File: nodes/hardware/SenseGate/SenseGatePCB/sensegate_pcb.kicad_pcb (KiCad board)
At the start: 2 copper layers, 110.1 x 110.1 mm, 24 parts, among them J3 Conn_01x02_Socket, J4 Conn_01x24_Pin, J5 Conn_01x04_Socket, J6 Conn_01x04_Socket, J7 Conn_01x04_Socket, J8 Conn_01x04_Socket, J9 Conn_01x04_Socket, Q4 SS8050, U1 DD05CVSA, U2 mt3608_dcdc_converter

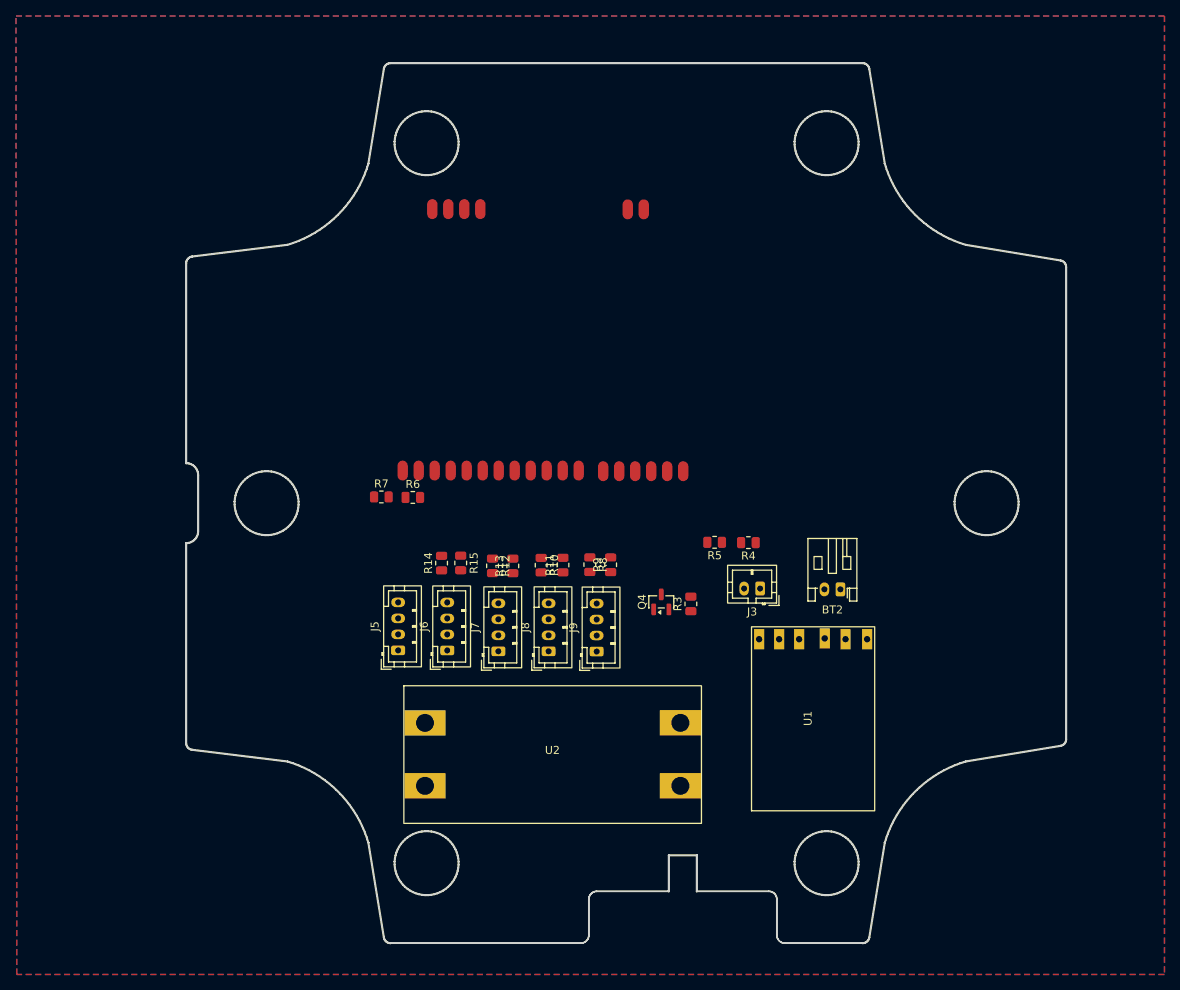
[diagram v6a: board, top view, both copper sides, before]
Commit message: pcb needs only wiring now
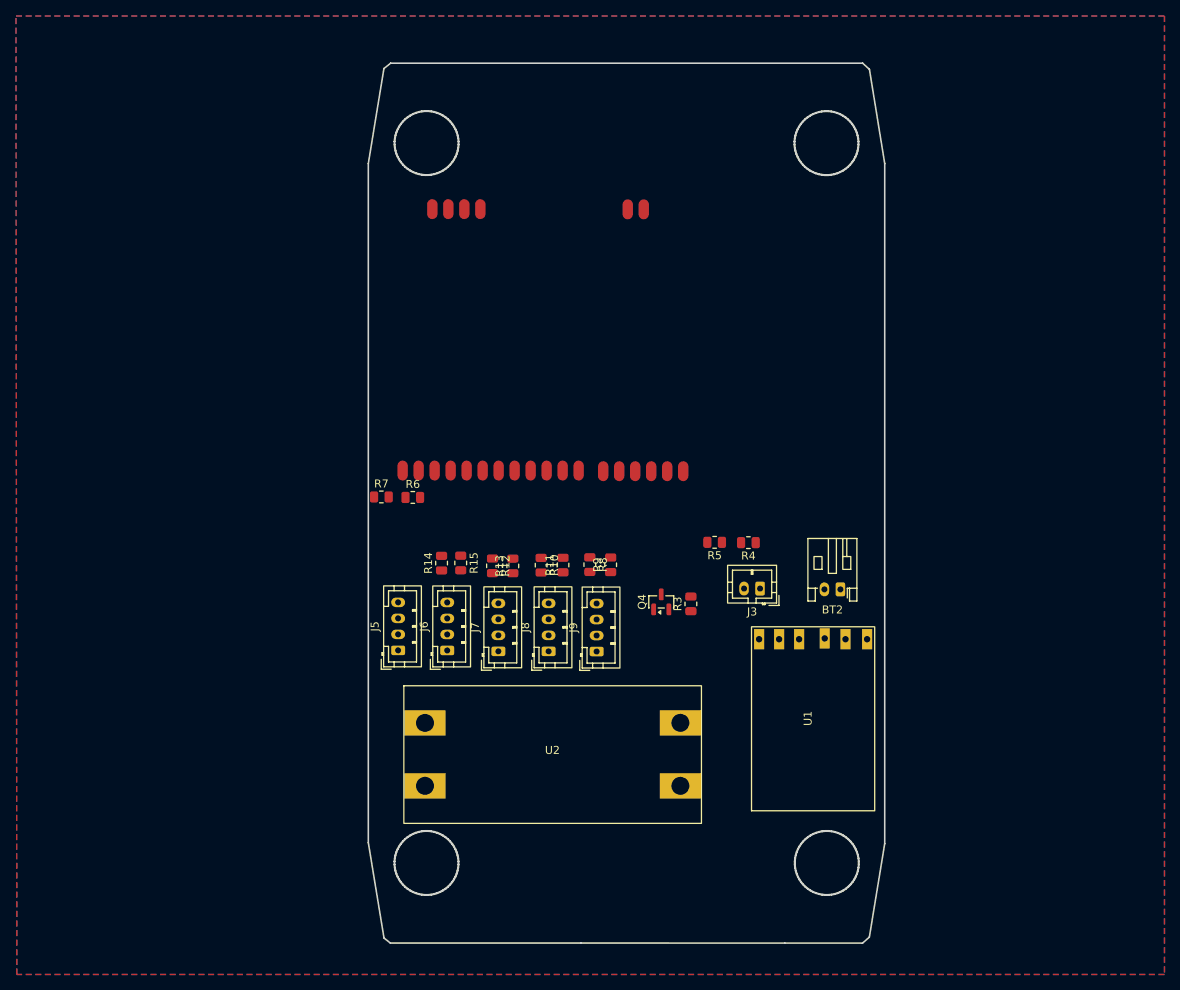
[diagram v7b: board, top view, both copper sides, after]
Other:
- board size 110.1 x 110.1 mm -> 64.6 x 110 mm

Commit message: wip
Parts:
- moved R14 8.84 mm to (113.3, 101.8), turned to -90 degrees
- moved R12 6.39 mm to (104.5, 101.9)
- moved R13 6.39 mm to (107.0, 101.9)
- moved R15 4.05 mm to (110.9, 101.8), turned to 90 degrees
- moved R7 1.08 mm to (97.5, 94.2), turned to 90 degrees
- turned R5 to 0 degrees
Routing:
- net VBAT: track 0.00 -> 132.0 mm, vias 0 -> 7
- net +3V3: track 0.00 -> 96.4 mm, vias 0 -> 5
- net TOG_20V: track 0.00 -> 32.1 mm, vias 0 -> 2
- net MON_SOLAR: track 0.00 -> 31.2 mm, vias 0 -> 2
- net reed_sw_03_measure: track 0.00 -> 25.8 mm, vias 0 -> 2
- net reed_sw_04_measure: track 0.00 -> 24.6 mm, vias 0 -> 2
- net GND_IS: track 0.00 -> 21.7 mm
- net reed_sw_01_measure: track 0.00 -> 20.5 mm
- net reed_sw_02_measure: track 0.00 -> 20.0 mm
- net Net-(J3-Pin_2): track 0.00 -> 14.8 mm
- net Net-(Q4-E): track 0.00 -> 14.8 mm
- net 20V: track 0.00 -> 14.5 mm, vias 0 -> 1
- net Net-(J5-Pin_4): track 0.00 -> 14.3 mm
- net Net-(J3-Pin_1): track 0.00 -> 13.3 mm, vias 0 -> 1
- net Net-(Q4-B): track 0.00 -> 7.98 mm, vias 0 -> 2
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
